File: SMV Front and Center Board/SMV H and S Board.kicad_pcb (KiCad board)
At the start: 2 copper layers, 57 parts, among them J1 430450200, J10 Molex Micro-Fit 4 Pin, J2 430450200, J3 XT60-M, J4 22035035, J5 22035035, J6 22035035, J7 22035035, Q1 PSMN1R8-40YLC_115, Q2 PSMN1R8-40YLC_115, U1 UA78M05QDCYRG4Q1, U3 PADS131M04QPWRQ1

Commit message: PCB Layout Draft and Small Schematic Changes
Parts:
- added TP19: 3V3A, TestPoint:TestPoint_Pad_D3.0mm, F.Cu at (99.0, 50.4)
- added TP20: 3V3A, TestPoint:TestPoint_Pad_D3.0mm, F.Cu at (106.3, 57.5)
- added TP21: 3V3A, TestPoint:TestPoint_Pad_D3.0mm, F.Cu at (100.0, 62.9)
- moved R9 128.3 mm to (122.5, 54.1), turned to 90 degrees
- moved R10 127.8 mm to (125.2, 53.5)
- moved R6 121.9 mm to (116.7, 49.6)
- moved C5 120.9 mm to (120.0, 50.5)
- moved R5 120.1 mm to (116.7, 47.0)
- moved C8 116.9 mm to (120.0, 45.9)
- moved R4 114.5 mm to (130.4, 52.0)
- moved C4 113.3 mm to (124.0, 43.5), turned to 0 degrees
- moved U3 111.7 mm to (125.5, 48.7)
- moved C1 108.7 mm to (131.8, 46.1), turned to 90 degrees
- moved C2 106.7 mm to (128.5, 42.8), turned to 90 degrees
- moved TP15 104.8 mm to (117.0, 31.5)
- moved TP4 102.7 mm to (104.0, 41.0)
- moved TP5 101.7 mm to (78.5, 68.0)
- moved TP11 80.5 mm to (183.5, 57.0)
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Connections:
- D2 pad 1: unconnected-(D2-Pad1) -> GND
- R11 pad 2: Net-(RP2040-A0) -> Net-(RP2040-D10)
- R12 pad 2: Net-(RP2040-A1) -> Net-(RP2040-D6)
- R7 pad 1: /D25 -> /D11
- R8 pad 1: /D4 -> /D12
- RP2040 pad 12: /PWM_OUT -> unconnected-(RP2040-SDA-Pad12)
- RP2040 pad 13: /D4 -> unconnected-(RP2040-D4-Pad13)
- RP2040 pad 16: /MISO -> unconnected-(RP2040-MISO-Pad16)
- RP2040 pad 17: /MOSI -> unconnected-(RP2040-MOSI-Pad17)
- RP2040 pad 19: /D25 -> unconnected-(RP2040-D25-Pad19)
- RP2040 pad 20: unconnected-(RP2040-D24-Pad20) -> /GPIO_RESET
- RP2040 pad 21: unconnected-(RP2040-A3-Pad21) -> /CS
- RP2040 pad 22: unconnected-(RP2040-A2-Pad22) -> /MISO
- RP2040 pad 23: Net-(RP2040-A1) -> /MOSI
- RP2040 pad 24: Net-(RP2040-A0) -> /GPIO_CLKIN
- RP2040 pad 4: /CS -> unconnected-(RP2040-D13-Pad4)
- RP2040 pad 5: unconnected-(RP2040-D12-Pad5) -> /D12
- RP2040 pad 6: /TX1 -> /D11
- RP2040 pad 7: unconnected-(RP2040-D10-Pad7) -> Net-(RP2040-D10)
- RP2040 pad 9: unconnected-(RP2040-D6-Pad9) -> Net-(RP2040-D6)
- U3 pad 11: /TX1 -> /GPIO_RESET
- U3 pad 17: /PWM_OUT -> /GPIO_CLKIN
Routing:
- net GND: track 69.2 -> 10.9 mm
- net Net-(U3-AIN3P): track 42.6 -> 3.34 mm
- net Net-(RP2040-A0): track 32.5 -> 0.00 mm
- net +12V: track 41.0 -> 15.2 mm
- net Net-(U3-AIN1P): track 30.6 -> 5.20 mm
- net +5V: track 24.8 -> 0.00 mm
- net +3V3: track 28.9 -> 4.64 mm
- net /D1: track 56.7 -> 33.2 mm
- net Net-(RP2040-A1): track 17.1 -> 0.00 mm
- net /CS: track 13.7 -> 1.96 mm
- net Net-(Q2-Pad4): track 10.8 -> 0.13 mm
- net Net-(U3-CAP): track 12.5 -> 3.27 mm
- net Net-(D3-Pad2): track 5.46 -> 0.00 mm
- net Net-(D2-Pad2): track 4.76 -> 0.00 mm
- net Net-(D1-Pad2): track 4.73 -> 0.00 mm
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- removed copper zone on F.Cu, net +3V3

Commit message: Formed compact subsystems
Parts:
- added D4: WL-SMCW_0603, SMV_Passives:WL-SMCW_0603(diode), F.Cu at (166.4, 45.6)
- added R17: RCS0603150RJNEA, 150Ω, SMV_Passives:0805RESC2012X60N, F.Cu at (164.0, 44.6)
- moved TP3 184.8 mm to (216.3, 53.0)
- moved J7 119.3 mm to (111.2, 40.5), turned to 180 degrees
- moved C7 119.0 mm to (171.2, 39.9)
- moved C6 119.0 mm to (164.9, 41.4)
- moved U1 119.0 mm to (166.4, 35.5)
- moved TP14 117.3 mm to (118.6, 26.6), turned to 180 degrees
- moved R15 100.8 mm to (117.3, 44.6), turned to 180 degrees
- moved R16 93.5 mm to (120.6, 44.6), turned to 0 degrees
- moved TP13 92.9 mm to (99.5, 49.5), turned to -90 degrees
- moved J4 91.3 mm to (112.4, 56.1), turned to -90 degrees
- moved R13 85.7 mm to (117.2, 51.2), turned to 0 degrees
- moved R14 79.1 mm to (120.6, 51.2), turned to 0 degrees
- moved D3 65.2 mm to (135.6, 30.3), turned to 0 degrees
- moved TP2 63.8 mm to (130.2, 65.3)
- moved R1 60.2 mm to (136.3, 32.7), turned to -90 degrees
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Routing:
- net /D1: track 33.2 -> 7.59 mm
- net Net-(J7-Pad3): track 24.1 -> 4.22 mm
- net /SCLK: track 0.00 -> 19.5 mm
- net Net-(J4-Pad3): track 17.4 -> 4.37 mm
- net /GPIO_CLKIN: track 0.00 -> 12.5 mm
- net /MOSI: track 0.00 -> 12.1 mm
- net +12V: track 15.2 -> 3.25 mm
- net /GPIO_RESET: track 0.00 -> 9.76 mm
- net +5V: track 0.00 -> 9.06 mm
- net /MISO: track 0.00 -> 8.29 mm
- net +3V3: track 4.64 -> 12.6 mm
- net /D2: track 0.00 -> 7.28 mm
- net /CS: track 1.96 -> 8.07 mm
- net GND: track 10.9 -> 14.6 mm
- net Net-(RP2040-D6): track 0.00 -> 3.49 mm
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
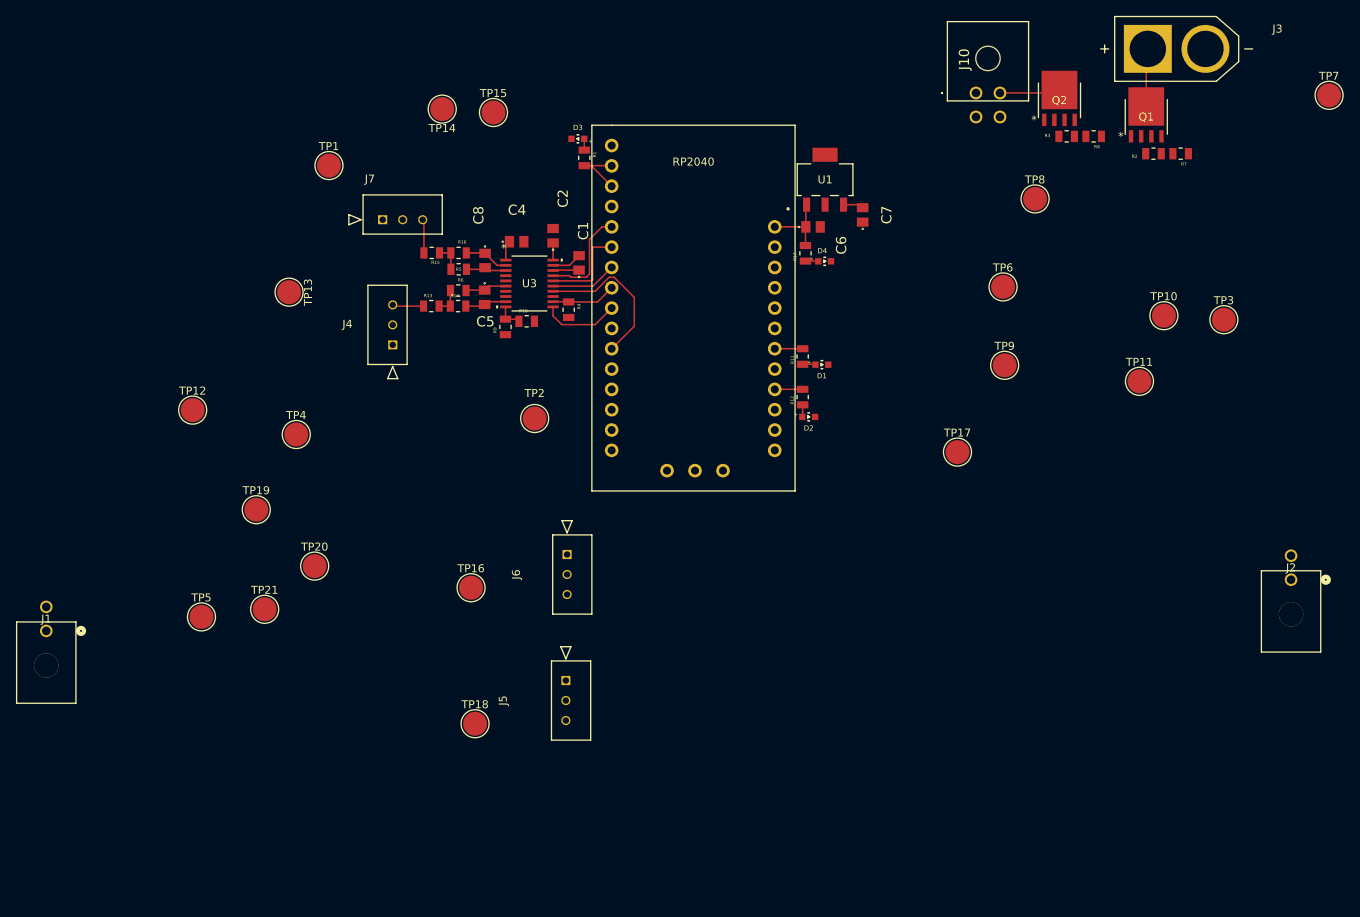
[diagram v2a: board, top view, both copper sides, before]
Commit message: Compacted wiper and horn connectors
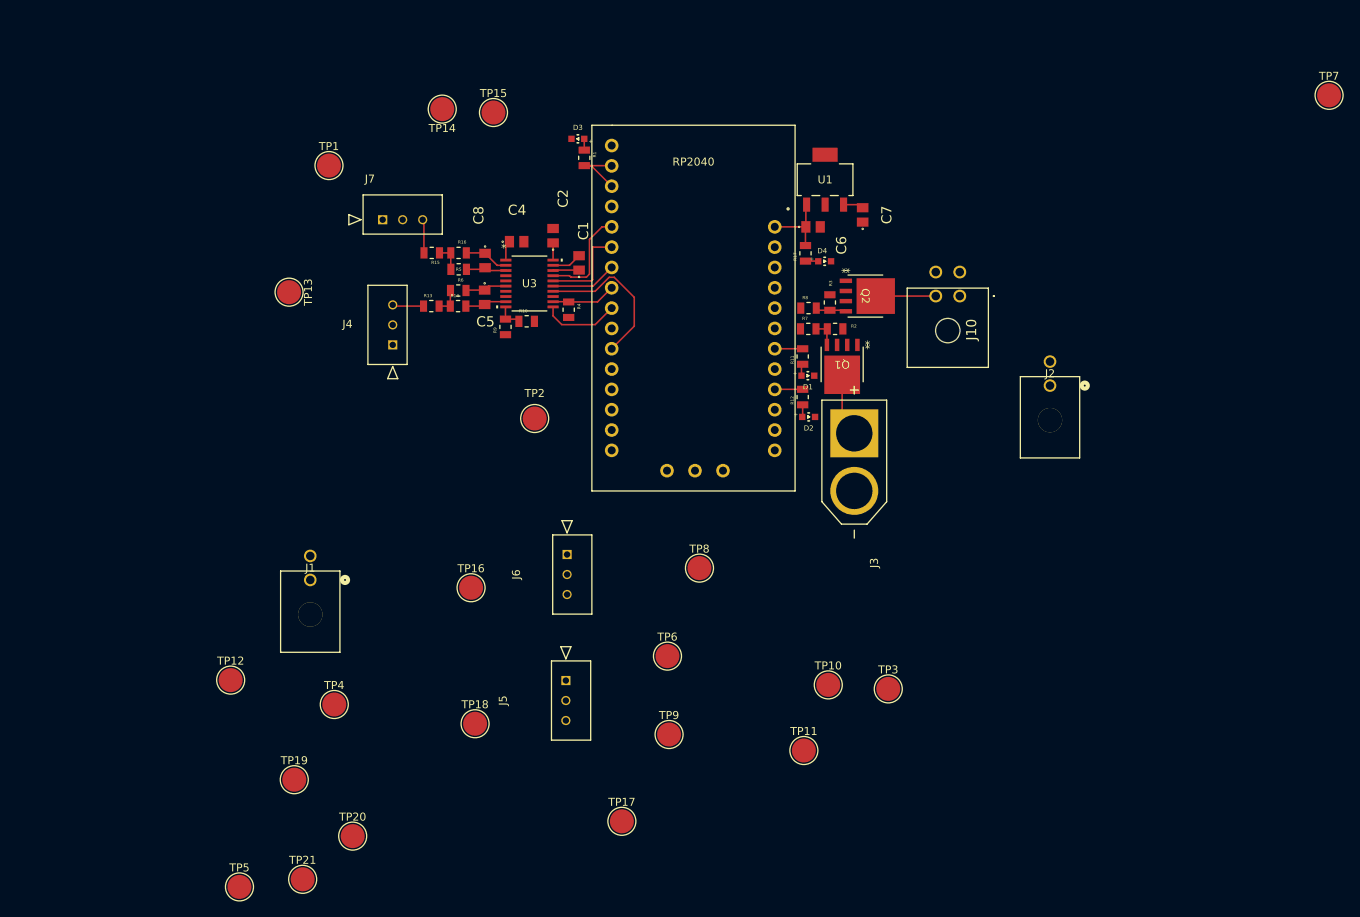
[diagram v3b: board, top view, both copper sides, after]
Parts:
- moved J3 65.5 mm to (170.1, 70.8), turned to -90 degrees
- moved TP10 62.4 mm to (166.8, 98.6)
- moved TP3 62.4 mm to (174.3, 99.1)
- moved TP9 62.4 mm to (146.9, 104.8)
- moved TP17 62.4 mm to (141.1, 115.7)
- moved TP11 62.4 mm to (163.8, 106.8)
- moved TP6 62.4 mm to (146.8, 95.0)
- moved TP8 62.4 mm to (150.8, 84.0)
- moved R7 51.4 mm to (164.3, 54.1), turned to 0 degrees
- moved Q1 49.0 mm to (168.6, 58.5), turned to 180 degrees
- moved R2 45.4 mm to (167.7, 54.1), turned to 180 degrees
- moved R8 41.6 mm to (164.4, 51.5), turned to 0 degrees
- moved J2 38.7 mm to (194.6, 61.2)
- moved R3 36.2 mm to (167.1, 50.8), turned to 90 degrees
- moved Q2 34.5 mm to (171.5, 50.0), turned to -90 degrees
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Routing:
- net Net-(Q2-Pad4): track 0.13 -> 3.87 mm
- net Net-(Q1-Pad4): track 0.00 -> 3.43 mm
- net /D2: track 7.28 -> 7.94 mm

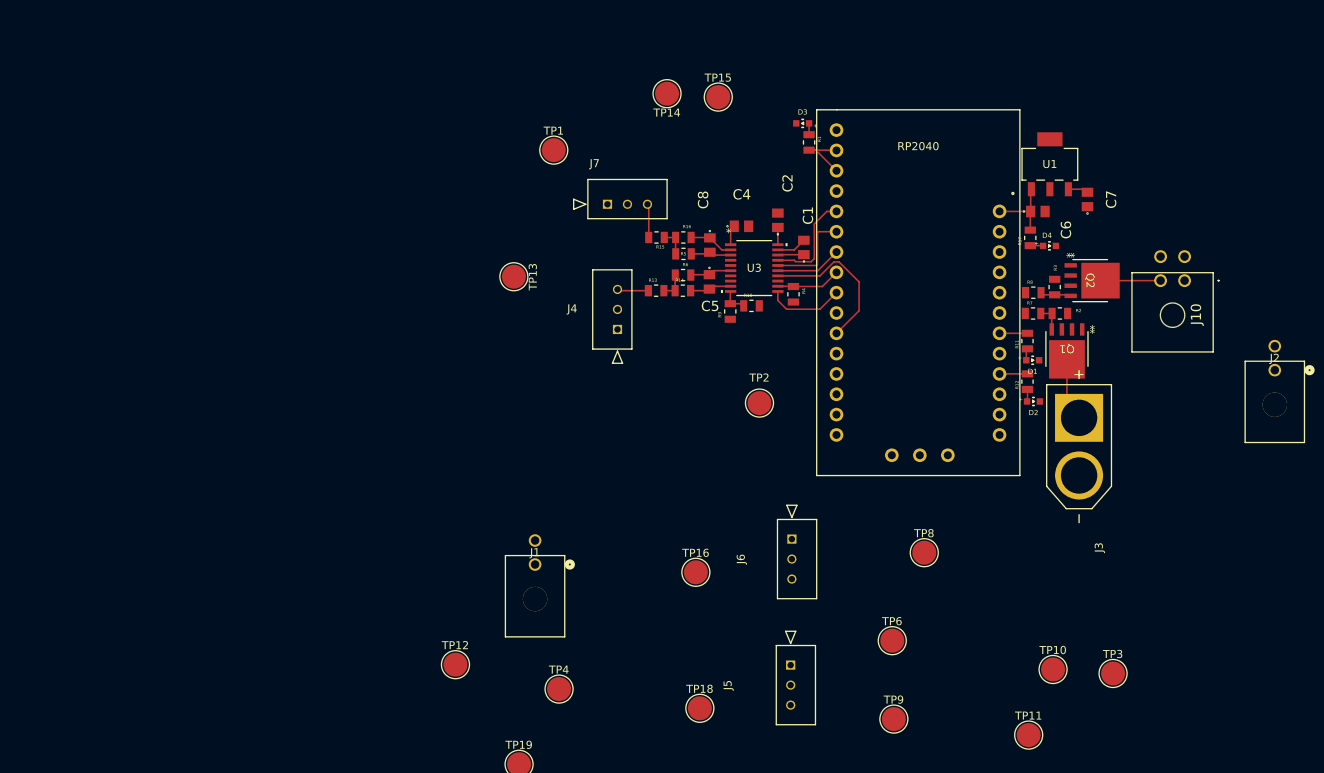
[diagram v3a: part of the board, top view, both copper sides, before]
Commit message: Added buffer and reorganized components
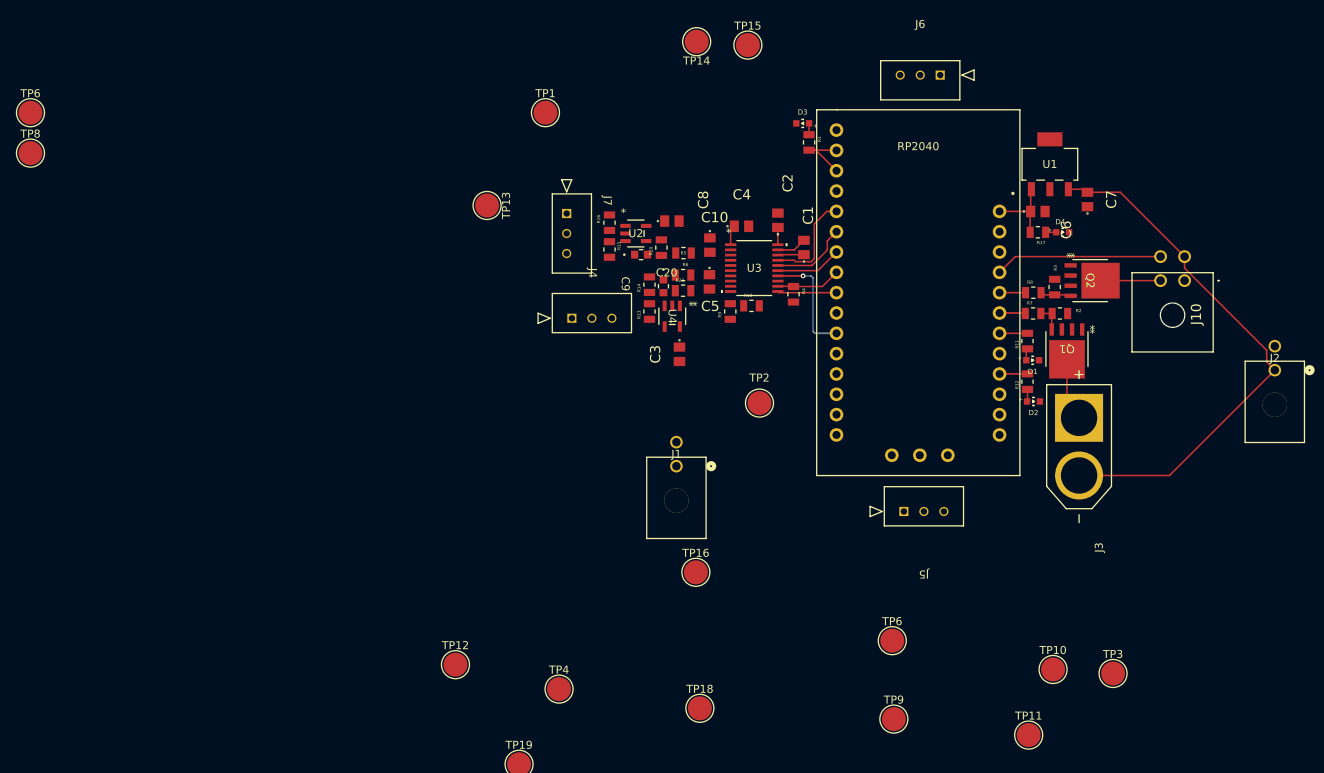
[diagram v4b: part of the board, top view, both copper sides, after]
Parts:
- added C10: 1uF,16V, SMV_Passives:Cap0805, F.Cu at (119.2, 42.5)
- added C20: 0603W475K250XD, SMV_Passives:CAP_0603-X_NGC, F.Cu at (115.3, 46.8)
- added C3: 1uF,16V, SMV_Passives:Cap0805, F.Cu at (120.2, 59.2)
- added C9: 0603W475K250XD, SMV_Passives:CAP_0603-X_NGC, F.Cu at (118.2, 50.7)
- added R20: 50Ω, SMV_Passives:0805RESC2012X60N, F.Cu at (117.9, 45.9)
- added R23: 50Ω, SMV_Passives:0805RESC2012X60N, F.Cu at (120.6, 51.2)
- added TP6: 12V, TestPoint:TestPoint_Pad_D3.0mm, F.Cu at (39.0, 29.0)
- added U2: MCP6286T-E/OT, SMV_ICs:SOT-23-5_MC_MCH, F.Cu at (114.7, 44.1)
- added U4: MCP6286T-E/OT, SMV_ICs:SOT-23-5_MC_MCH, F.Cu at (119.2, 54.4)
- moved TP8 122.4 mm to (39.0, 34.1)
- moved J6 60.9 mm to (152.7, 24.3), turned to 0 degrees
- moved J5 23.9 mm to (148.2, 78.8), turned to 180 degrees
- moved J1 21.5 mm to (119.8, 73.2)
- moved TP13 9.52 mm to (96.1, 40.6)
- moved R16 9.42 mm to (111.4, 42.8), turned to 90 degrees
- moved TP14 7.48 mm to (122.3, 20.1)
- moved TP15 7.48 mm to (128.7, 20.6)
- moved R15 6.07 mm to (111.4, 46.1), turned to -90 degrees
- moved J4 5.87 mm to (106.7, 54.7), turned to 180 degrees
- moved J7 5.23 mm to (106.1, 41.6), turned to 90 degrees
- moved TP1 4.80 mm to (103.4, 29.0)
- moved R14 4.24 mm to (116.4, 50.5), turned to 90 degrees
- moved R13 2.73 mm to (116.4, 53.9), turned to 90 degrees
- moved D4 2.37 mm to (168.1, 44.0)
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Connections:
- net /D1 renamed /Drain1
- net /D2 renamed /Drain2
- C7 pad 2: +12V -> Net-(U1-INPUT)
- J10 pad 1: GND -> unconnected-(J10-Pad1)
- J10 pad 3: GND -> +12V
- J10 pad 4: +12V -> /D13
- J4 pad 1: +3.3V -> +3V3
- J7 pad 1: +3.3V -> +3V3
- Q2 pad 1: GND - S -> GND
- Q2 pad 2: GND - S -> GND
- Q2 pad 3: GND - S -> GND
- R5 pad 2: /HS1 -> /ADC_IN1
- R6 pad 2: /HS2 -> /ADC_IN2
- RP2040 pad 4: unconnected-(RP2040-D13-Pad4) -> /D13
- TP2 pad 1: +12V -> Net-(U1-INPUT)
- U1 pad 3: +12V -> Net-(U1-INPUT)
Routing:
- net +12V: track 3.25 -> 67.5 mm
- net /D13: track 0.00 -> 20.9 mm
- net GND: track 14.6 -> 4.60 mm
- net /SCLK: track 19.5 -> 14.2 mm, vias 0 -> 1
- net Net-(U3-AIN1P): track 5.20 -> 0.78 mm
- net Net-(U3-AIN0P): track 5.15 -> 0.78 mm
- net Net-(J4-Pad3): track 4.37 -> 0.00 mm
- net Net-(J7-Pad3): track 4.22 -> 0.00 mm
- net /HS2: track 3.37 -> 0.00 mm
- net /HS1: track 3.47 -> 0.11 mm
- net /D12: track 0.00 -> 3.25 mm
- net /D11: track 0.00 -> 3.24 mm
- net Net-(U3-AIN3P): track 3.34 -> 0.44 mm
- net /GPIO_RESET: track 9.76 -> 7.39 mm
- net /MOSI: track 12.1 -> 10.4 mm

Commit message: Reorganized
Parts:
- removed TP10: 5V, TestPoint:TestPoint_Pad_D3.0mm
- removed TP6 (x2), TP7: 12V, TestPoint:TestPoint_Pad_D3.0mm
- moved TP8 136.0 mm to (175.0, 33.5)
- moved TP9 87.2 mm to (190.0, 29.0)
- moved TP12 76.4 mm to (124.0, 28.5)
- moved TP17 74.6 mm to (215.7, 118.3)
- moved TP5 72.9 mm to (125.5, 58.5)
- moved TP3 66.3 mm to (180.0, 33.0)
- moved TP21 64.9 mm to (128.5, 64.0)
- moved TP15 64.5 mm to (72.9, 52.9)
- moved J6 58.8 mm to (185.4, 73.3), turned to 90 degrees
- moved TP2 56.1 mm to (180.0, 39.5)
- moved J3 55.9 mm to (190.0, 18.5), turned to 180 degrees
- moved J1 49.6 mm to (99.4, 27.9)
- moved TP18 49.3 mm to (73.4, 104.5)
- moved J5 46.4 mm to (102.2, 73.3), turned to 90 degrees
- moved TP14 40.2 mm to (92.5, 47.0)
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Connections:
- net Net-(U2-VIN-) renamed /FB
- C7 pad 2: Net-(U1-INPUT) -> +12V
- J1 pad 1: unconnected-(J1-Pad1) -> GND
- J1 pad 2: unconnected-(J1-Pad2) -> +12V
- TP2 pad 1: Net-(U1-INPUT) -> +12V
- U1 pad 3: Net-(U1-INPUT) -> +12V
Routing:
- net /CAN_L: track 0.00 -> 88.5 mm
- net /CAN_H: track 0.00 -> 87.4 mm
- net +12V: track 67.5 -> 0.00 mm
- net /Drain2: track 7.94 -> 53.3 mm
- net Net-(J4-Pad3): track 0.00 -> 22.4 mm
- net /Drain1: track 7.51 -> 29.0 mm
- net /D13: track 20.9 -> 39.5 mm
- net Net-(J7-Pad3): track 0.00 -> 13.0 mm
- net +3V3: track 12.6 -> 0.04 mm
- net Net-(U3-AIN3P): track 0.44 -> 9.85 mm
- net +5V: track 9.34 -> 0.00 mm
- net /GPIO_RESET: track 7.39 -> 15.5 mm
- net Net-(U4-VIN-): track 0.00 -> 5.80 mm
- net /HS2: track 0.00 -> 5.68 mm
- net /FB: track 0.48 -> 5.78 mm
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- added copper zone on F.Cu, net +12V
- added copper zone on F.Cu, net +5V

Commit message: Organized testpoints and added polygons
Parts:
- removed TP15: 3V3D, TestPoint:TestPoint_Pad_D3.0mm
- removed TP4: 3V3A, TestPoint:TestPoint_Pad_D3.0mm
- moved TP17 107.1 mm to (134.5, 48.5)
- moved TP19 63.2 mm to (134.0, 60.5)
- moved TP20 57.9 mm to (129.0, 64.0)
- moved TP18 46.4 mm to (107.5, 73.0)
- moved TP11 44.5 mm to (135.0, 44.0)
- moved TP16 37.9 mm to (107.5, 78.5)
- moved TP1 27.8 mm to (102.5, 30.0)
- moved TP21 11.8 mm to (131.0, 52.5)
- moved J5 11.7 mm to (90.5, 73.3)
- moved TP13 11.0 mm to (99.5, 55.5)
- moved J1 8.14 mm to (91.3, 27.9)
- moved J4 8.14 mm to (90.5, 57.0)
- moved J7 8.14 mm to (90.5, 42.1)
- moved J6 6.69 mm to (192.0, 73.3)
- moved TP14 5.55 mm to (98.0, 47.0)
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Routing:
- net /CAN_L: track 88.5 -> 107.1 mm
- net /CAN_H: track 87.4 -> 103.7 mm
- net /CS: track 12.7 -> 28.8 mm, vias 0 -> 2
- net /GPIO_RESET: track 15.5 -> 29.9 mm
- net /MISO: track 12.8 -> 16.4 mm
- net /GPIO_CLKIN: track 14.4 -> 17.9 mm
- net Net-(J4-Pad3): track 22.4 -> 19.1 mm
- net /MOSI: track 14.3 -> 17.2 mm
- net Net-(U3-CAP): track 3.47 -> 6.09 mm
- net Net-(J7-Pad3): track 13.0 -> 12.4 mm
- added copper zone on F.Cu, net +3V3
- added copper zone on B.Cu, net GND

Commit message: Reorganized, added filled zones
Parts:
- removed J3: XT60-M, XT60-M:AMASS_XT60-M
- removed TP20: 3V3A, TestPoint:TestPoint_Pad_D3.0mm
- added J8: 430450200, SMV_Connectors:CONN_SD-43045-001_02_MOL, F.Cu at (182.6, 60.3)
- added TP15: 3V3A, TestPoint:TestPoint_Pad_D1.5mm, F.Cu at (135.5, 42.5)
- Horn: renamed from TP9; footprint TestPoint:TestPoint_Pad_D3.0mm -> TestPoint:TestPoint_Pad_D1.5mm
- TP11, TP13, TP14, TP16, TP17, TP18, TP19, TP21, TP3, TP5: footprint TestPoint:TestPoint_Pad_D3.0mm -> TestPoint:TestPoint_Pad_D1.5mm
- Wipers: renamed from TP8; footprint TestPoint:TestPoint_Pad_D3.0mm -> TestPoint:TestPoint_Pad_D1.5mm
- moved J1 97.6 mm to (188.7, 32.8), turned to 180 degrees
- moved Horn 36.2 mm to (174.0, 61.5)
- moved J2 33.7 mm to (187.7, 74.2)
- moved J10 22.3 mm to (182.7, 43.0), turned to 90 degrees
- moved J6 22.1 mm to (170.0, 74.0)
- moved Wipers 19.3 mm to (179.5, 52.3)
- moved TP3 16.4 mm to (164.5, 38.5)
- moved J4 6.47 mm to (97.0, 57.0)
- moved J5 6.47 mm to (97.0, 73.3)
- moved J7 6.47 mm to (97.0, 42.1)
- moved TP13 6.47 mm to (106.0, 55.5)
- moved TP14 6.42 mm to (104.4, 47.5)
- moved C3 6.05 mm to (118.4, 59.0), turned to 0 degrees
- moved C1 5.39 mm to (132.4, 45.0)
- moved C9 5.19 mm to (114.1, 51.2)
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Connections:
- RP2040 pad 17: unconnected-(RP2040-MOSI-Pad17) -> /GPIO_RESET
- RP2040 pad 19: unconnected-(RP2040-D25-Pad19) -> /CS
- RP2040 pad 20: /GPIO_RESET -> unconnected-(RP2040-D24-Pad20)
- RP2040 pad 21: /CS -> unconnected-(RP2040-A3-Pad21)
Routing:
- net /Drain2: track 53.3 -> 5.52 mm
- net /GPIO_RESET: track 29.9 -> 0.00 mm
- net /CAN_L: track 107.1 -> 78.9 mm
- net /CAN_H: track 103.7 -> 76.0 mm
- net /D13: track 39.5 -> 20.8 mm
- net +5V: track 0.00 -> 14.4 mm
- net /Drain1: track 29.0 -> 15.0 mm
- net +3V3: track 0.04 -> 10.5 mm
- net /CS: track 28.8 -> 21.7 mm, vias 2 -> 0
- net /MOSI: track 17.2 -> 12.2 mm
- net /MISO: track 16.4 -> 12.9 mm
- net /GPIO_CLKIN: track 17.9 -> 14.9 mm
- net Net-(U3-CAP): track 6.09 -> 3.41 mm
- net Net-(U3-AIN3P): track 9.85 -> 7.18 mm
- net /SCLK: track 18.6 -> 20.7 mm, vias 1 -> 0
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- removed copper zone on F.Cu, net +5V
